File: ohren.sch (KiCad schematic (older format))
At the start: 34 parts, among them J1 Conn_01x18_Male, U1 TLC5951RHA, U2 TLC5951RHA

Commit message: WIP
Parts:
- D10, D11, D12, D14, D15, D17, D4, D5, D6, D7, D8, D9: symbol Device:LED_ARGB -> LED:ASMB-MTB1-0A3A2
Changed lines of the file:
@@
 U1_B1
 $Comp
-L Device:LED_ARGB D6
+L LED:ASMB-MTB1-0A3A2 D6
 U 1 1 5C9EA530
 P 4850 3400
@@
 U1_B2
 $Comp
-L Device:LED_ARGB D7
+L LED:ASMB-MTB1-0A3A2 D7
 U 1 1 5C9EA53F
 P 4850 4250
@@
 	4300 6050 4200 5950
 $Comp
-L Device:LED_ARGB D4
+L LED:ASMB-MTB1-0A3A2 D4
 U 1 1 5CA0D84C
 P 5950 4250
@@
 U1_B4
 $Comp
-L Device:LED_ARGB D5
+L LED:ASMB-MTB1-0A3A2 D5
 U 1 1 5CA0D85B
 P 4850 6150
@@
 	4300 6500 5400 6500
 $Comp
-L Device:LED_ARGB D8
+L LED:ASMB-MTB1-0A3A2 D8
 U 1 1 5CA14C02
 P 5950 5300
@@
 U1_B6
 $Comp
-L Device:LED_ARGB D9
+L LED:ASMB-MTB1-0A3A2 D9
 U 1 1 5CA14C11
 P 5950 6150
@@
 Connection ~ 6300 5300
 $Comp
-L Device:LED_ARGB D10
+L LED:ASMB-MTB1-0A3A2 D10
 U 1 1 5CA31CCE
 P 10450 6150
@@
 U2_B0
 $Comp
-L Device:LED_ARGB D11
+L LED:ASMB-MTB1-0A3A2 D11
 U 1 1 5CA31D33
 P 10450 5300
@@
 U2_B1
 $Comp
-L Device:LED_ARGB D14
+L LED:ASMB-MTB1-0A3A2 D14
 U 1 1 5CA31D42
 P 9350 6150
@@
 U2_B6
 $Comp
-L Device:LED_ARGB D17
+L LED:ASMB-MTB1-0A3A2 D17
 U 1 1 5CA31DD4
 P 9350 3400
@@
 	3700 1200 4000 1200
 $Comp
-L Device:LED_ARGB D15
+L LED:ASMB-MTB1-0A3A2 D15
 U 1 1 5CA31D51
 P 10450 4250
@@
 	8900 4050 9150 4050
 $Comp
-L Device:LED_ARGB D12
+L LED:ASMB-MTB1-0A3A2 D12
 U 1 1 5CA31D9B
 P 10450 3400
@@
 Wire Wire Line
 	4550 1300 4250 1300
+Connection ~ 4550 1000
+Connection ~ 4550 1300
 Wire Bus Line
 	5400 2750 5400 4550
@@
 Wire Bus Line
 	2350 3050 2350 6850
-Connection ~ 4550 1000
-Connection ~ 4550 1300
 $EndSCHEMATC

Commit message: WIP
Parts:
- removed D17: LED_ARGB, LED_SMD:LED_Cree-PLCC4_3.2x2.8mm_CCW, symbol LED:ASMB-MTB1-0A3A2
- removed J1: Conn_01x18_Male, catear-pcb:solder_conn18, symbol Connector:Conn_01x18_Male
- added D1, D2: LED, catear-pcb:smd_led_universal, symbol Device:LED
- added D13, D3: LED_ARGB, LED_SMD:LED_Cree-PLCC4_3.2x2.8mm_CCW, symbol LED:ASMB-MTB1-0A3A2
- added J1: Conn_01x19_MountingPin, catear-pcb:Molex_Easy-On_54550-1971_1x19_P0.5mm_Horizontal, symbol Connector_Generic_MountingPin:Conn_01x19_MountingPin
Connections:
- wire segments 244 -> 247
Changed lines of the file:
@@
 Text Label 10000 5500 0    50   ~ 0
 U2_B6
-$Comp
-L LED:ASMB-MTB1-0A3A2 D17
-U 1 1 5CA31DD4
-P 9350 3400
-F 0 "D17" H 9350 3897 50  0000 C CNN
-F 1 "LED_ARGB" H 9350 3806 50  0000 C CNN
-F 2 "LED_SMD:LED_Cree-PLCC4_3.2x2.8mm_CCW" H 9350 3350 50  0001 C CNN
-F 3 "~" H 9350 3350 50  0001 C CNN
-	1    9350 3400
-	1    0    0    -1
-$EndComp
 Entry Wire Line
 	9900 6050 10000 5950
@@
 	5500 4450 5750 4450
 Wire Wire Line
-	1300 1200 1900 1200
+	1300 1200 1600 1200
 Text Label 3700 1750 1    50   ~ 0
 U1_G4
@@
 Wire Wire Line
 	2500 1500 2500 1750
-$Comp
-L Connector:Conn_01x18_Male J1
-U 1 1 5CDF8D04
-P 550 2200
-F 0 "J1" V 385 2128 50  0000 C CNN
-F 1 "Conn_01x18_Male" V 476 2128 50  0000 C CNN
-F 2 "catear-pcb:solder_conn18" H 550 2200 50  0001 C CNN
-F 3 "~" H 550 2200 50  0001 C CNN
-	1    550  2200
-	0    1    1    0
-$EndComp
 Wire Wire Line
 	-350 2400 -350 2550
@@
 	1800 2550 1800 2250
 Wire Wire Line
-	1800 2550 1350 2550
+	1800 2550 1650 2550
 Wire Wire Line
 	1250 2550 1250 2400
@@
 	1050 2400 1050 2750
 Wire Wire Line
-	2000 2650 950  2650
-Wire Wire Line
 	950  2650 950  2400
 Wire Wire Line
@@
 Connection ~ 4550 1000
 Connection ~ 4550 1300
+$Comp
+L Connector_Generic_MountingPin:Conn_01x19_MountingPin J1
+U 1 1 5CBA6D41
+P 550 2200
+F 0 "J1" V 775 2118 50  0000 C CNN
+F 1 "Conn_01x19_MountingPin" V 684 2118 50  0000 C CNN
+F 2 "catear-pcb:Molex_Easy-On_54550-1971_1x19_P0.5mm_Horizontal" H 550 2200 50  0001 C CNN
+F 3 "~" H 550 2200 50  0001 C CNN
+	1    550  2200
+	0    -1   -1   0
+$EndComp
+$Comp
+L Device:LED D2
+U 1 1 5CBB1488
+P 1600 1350
+F 0 "D2" V 1639 1233 50  0000 R CNN
+F 1 "LED" V 1548 1233 50  0000 R CNN
+F 2 "catear-pcb:smd_led_universal" H 1600 1350 50  0001 C CNN
+F 3 "~" H 1600 1350 50  0001 C CNN
+	1    1600 1350
+	0    -1   -1   0
+$EndComp
+Connection ~ 1600 1200
+Wire Wire Line
+	1600 1200 1900 1200
+$Comp
+L Device:LED D1
+U 1 1 5CBB1D47
+P 1300 1350
+F 0 "D1" V 1339 1233 50  0000 R CNN
+F 1 "LED" V 1248 1233 50  0000 R CNN
+F 2 "catear-pcb:smd_led_universal" H 1300 1350 50  0001 C CNN
+F 3 "~" H 1300 1350 50  0001 C CNN
+	1    1300 1350
+	0    -1   -1   0
+$EndComp
+Connection ~ 1300 1200
+$Comp
+L LED:ASMB-MTB1-0A3A2 D3
+U 1 1 5CBB4B97
+P 5950 3400
+F 0 "D3" H 5950 3897 50  0000 C CNN
+F 1 "LED_ARGB" H 5950 3806 50  0000 C CNN
+F 2 "LED_SMD:LED_Cree-PLCC4_3.2x2.8mm_CCW" H 5950 3350 50  0001 C CNN
+F 3 "~" H 5950 3350 50  0001 C CNN
+	1    5950 3400
+	1    0    0    -1
+$EndComp
+$Comp
+L LED:ASMB-MTB1-0A3A2 D13
+U 1 1 5CBB539C
+P 9350 4250
+F 0 "D13" H 9350 4747 50  0000 C CNN
+F 1 "LED_ARGB" H 9350 4656 50  0000 C CNN
+F 2 "LED_SMD:LED_Cree-PLCC4_3.2x2.8mm_CCW" H 9350 4200 50  0001 C CNN
+F 3 "~" H 9350 4200 50  0001 C CNN
+	1    9350 4250
+	1    0    0    -1
+$EndComp
+Wire Wire Line
+	950  2650 2000 2650
+Wire Wire Line
+	1650 2550 1650 2200
 Wire Bus Line
 	5400 2750 5400 4550
@@
 Wire Bus Line
 	2350 3050 2350 6850
+Connection ~ 1650 2550
+Wire Wire Line
+	1650 2550 1350 2550
 $EndSCHEMATC

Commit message: Almost (tm) finish full rerouting
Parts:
- removed D1, D2: LED, catear-pcb:smd_led_universal, symbol Device:LED
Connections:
- wire segments 247 -> 246
- no-connect marks 1 -> 0
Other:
- moved on the sheet: D10, D11, D12, D13, D14, D15, D3, D4, D5, D6, D8, D9

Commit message: Finish layouting
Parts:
- removed C10, C9: C, Capacitor_SMD:C_1206_3216Metric, symbol Device:C
- removed C6: C, Capacitor_SMD:C_1210_3225Metric, symbol Device:C
- added C6: C, Capacitor_SMD:C_1210_3225Metric, symbol Device:C
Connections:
- wire segments 246 -> 245
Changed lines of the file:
@@
 Wire Wire Line
 	7350 4150 6950 4150
-$Comp
-L Device:C C6
-U 1 1 5C9DBD6E
-P 5150 1150
-F 0 "C6" H 5265 1196 50  0000 L CNN
-F 1 "C" H 5265 1105 50  0000 L CNN
-F 2 "Capacitor_SMD:C_1210_3225Metric" H 5188 1000 50  0001 C CNN
-F 3 "~" H 5150 1150 50  0001 C CNN
-	1    5150 1150
-	1    0    0    -1
-$EndComp
 Wire Wire Line
 	5150 900  5150 1000
@@
 Text Label 1800 3150 0    50   ~ 0
 DCSOUT
-Text Label 1800 3450 0    50   ~ 0
+Text Label 1800 3750 0    50   ~ 0
 GSSIN
-Text Label 1800 3350 0    50   ~ 0
+Text Label 1800 3650 0    50   ~ 0
 DCSIN
 Text Label 1800 3550 0    50   ~ 0
 GSSCK
-Text Label 1450 4400 0    50   ~ 0
+Text Label 1800 3450 0    50   ~ 0
 DCSCK
-Text Label 1800 4500 0    50   ~ 0
+Text Label 1800 3350 0    50   ~ 0
 XBLNK
-Text Label 1800 3750 0    50   ~ 0
+Text Label 1800 3950 0    50   ~ 0
 GSCKR
-Text Label 1800 3850 0    50   ~ 0
+Text Label 1800 4050 0    50   ~ 0
 GSCKG
-Text Label 1800 3950 0    50   ~ 0
+Text Label 1800 4150 0    50   ~ 0
 GSCKB
 Entry Wire Line
@@
 Entry Wire Line
 	2350 4350 2450 4250
-$Comp
-L Device:C C9
-U 1 1 5D009474
-P 4550 1150
-F 0 "C9" H 4668 1196 50  0000 L CNN
-F 1 "C" H 4668 1105 50  0000 L CNN
-F 2 "Capacitor_SMD:C_1206_3216Metric" H 4588 1000 50  0001 C CNN
-F 3 "~" H 4550 1150 50  0001 C CNN
-	1    4550 1150
-	1    0    0    -1
-$EndComp
-$Comp
-L Device:C C10
-U 1 1 5D01A6A4
-P 6050 1150
-F 0 "C10" H 6168 1196 50  0000 L CNN
-F 1 "C" H 6168 1105 50  0000 L CNN
-F 2 "Capacitor_SMD:C_1206_3216Metric" H 6088 1000 50  0001 C CNN
-F 3 "~" H 6050 1150 50  0001 C CNN
-	1    6050 1150
-	1    0    0    -1
-$EndComp
-Wire Wire Line
-	6050 1000 5750 1000
-Connection ~ 5750 1000
-Wire Wire Line
-	6050 1300 5750 1300
-Connection ~ 5750 1300
-Wire Wire Line
-	4850 1000 4550 1000
 Connection ~ 4850 1000
-Wire Wire Line
-	4850 1300 4550 1300
 Connection ~ 4850 1300
 $Comp
@@
 	1800 2550 1800 2250
 Wire Wire Line
-	1800 2550 1650 2550
-Wire Wire Line
 	1350 2400 1350 2550
 Wire Wire Line
@@
 	1900 2850 1900 2750
 Wire Wire Line
-	1900 2750 1250 2750
+	1900 2750 1700 2750
 Connection ~ 1250 2750
 Wire Wire Line
@@
 Wire Wire Line
 	2000 2250 2000 2650
-Text Label 1800 3650 0    50   ~ 0
+Text Label 1800 3850 0    50   ~ 0
 GSLAT
 Wire Wire Line
-	2250 3350 650  3350
-Wire Wire Line
-	650  3350 650  2400
-Wire Wire Line
-	2250 3450 550  3450
-Wire Wire Line
-	550  3450 550  2400
-Wire Wire Line
-	2250 3550 450  3550
-Wire Wire Line
-	450  3550 450  2400
-Wire Wire Line
-	2250 3650 350  3650
-Wire Wire Line
-	350  3650 350  2400
-Wire Wire Line
-	2250 3750 250  3750
-Wire Wire Line
-	250  3750 250  2400
-Wire Wire Line
 	2250 3850 250  3850
 Wire Wire Line
-	250  3850 250  3750
-Connection ~ 250  3750
-Wire Wire Line
-	2250 3950 250  3950
-Wire Wire Line
-	250  3950 250  3850
-Connection ~ 250  3850
-Wire Wire Line
-	2250 4050 150  4050
-Wire Wire Line
-	150  4050 150  2400
-Wire Wire Line
 	2250 4150 50   4150
-Wire Wire Line
-	50   4150 50   2400
 Text Label 1900 1750 1    50   ~ 0
 U2_R4
@@
 	1    0    0    -1
 $EndComp
-Wire Wire Line
-	4550 1000 4250 1000
-Wire Wire Line
-	4550 1300 4250 1300
-Connection ~ 4550 1000
-Connection ~ 4550 1300
 $Comp
 L Connector_Generic_MountingPin:Conn_01x19_MountingPin J1
@@
 $EndComp
 Wire Wire Line
-	1650 2550 1650 2200
-Connection ~ 1650 2550
-Wire Wire Line
-	1650 2550 1450 2550
-Wire Wire Line
 	1300 1200 1900 1200
 Wire Wire Line
@@
 Wire Wire Line
 	950  3250 950  2400
+Wire Wire Line
+	50   4150 50   4050
+Connection ~ 50   4050
+Wire Wire Line
+	50   4050 50   3950
+Wire Wire Line
+	50   3950 2250 3950
+Connection ~ 50   3950
+Wire Wire Line
+	50   3950 50   2400
+Wire Wire Line
+	-50  2650 150  2650
+Wire Wire Line
+	150  2650 150  2400
+Connection ~ -50  2650
+Wire Wire Line
+	50   4050 2250 4050
+Wire Wire Line
+	250  3850 250  2400
+Wire Wire Line
+	2250 3750 350  3750
+Wire Wire Line
+	350  3750 350  2400
+Wire Wire Line
+	2250 3650 450  3650
+Wire Wire Line
+	450  3650 450  2400
+Wire Wire Line
+	2250 3550 550  3550
+Wire Wire Line
+	550  3550 550  2400
+Wire Wire Line
+	2250 3450 650  3450
+Wire Wire Line
+	650  3450 650  2400
+Wire Wire Line
+	2250 3350 750  3350
+Wire Wire Line
+	750  3350 750  2400
+Wire Wire Line
+	1450 2550 1800 2550
+Wire Wire Line
+	1650 2200 1700 2200
+Wire Wire Line
+	1700 2200 1700 2750
+Connection ~ 1700 2750
+Wire Wire Line
+	1700 2750 1250 2750
+Wire Wire Line
+	4250 1000 4850 1000
+Wire Wire Line
+	4250 1300 4850 1300
+$Comp
+L Device:C C6
+U 0 0 5D11A988
+P 5150 1150
+F 0 "C6" H 5265 1196 50  0000 L CNN
+F 1 "C" H 5265 1105 50  0000 L CNN
+F 2 "Capacitor_SMD:C_1210_3225Metric" H 5188 1000 50  0001 C CNN
+F 3 "~" H 5150 1150 50  0001 C CNN
+	0    5150 1150
+	1    0    0    -1
+$EndComp
 Wire Bus Line
 	5400 2750 5400 4550

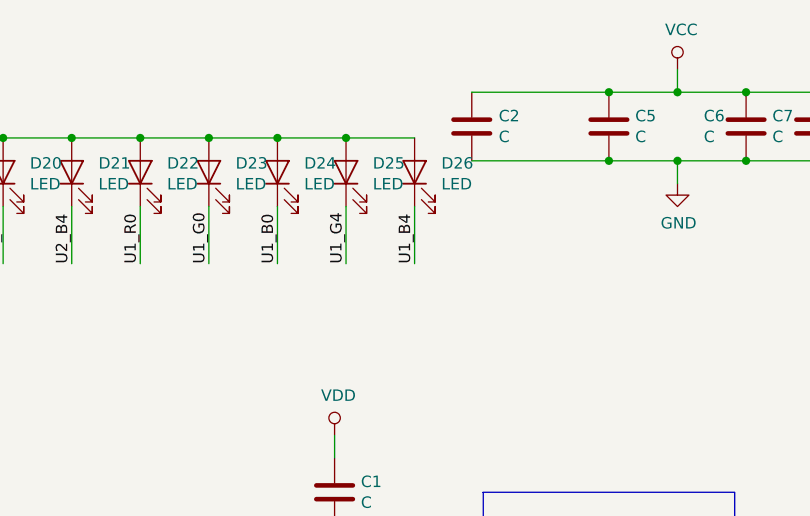
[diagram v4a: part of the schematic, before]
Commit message: Adjust UV LED attachment + U1 LED routing slightly
Slight changes for better groundplane coverage
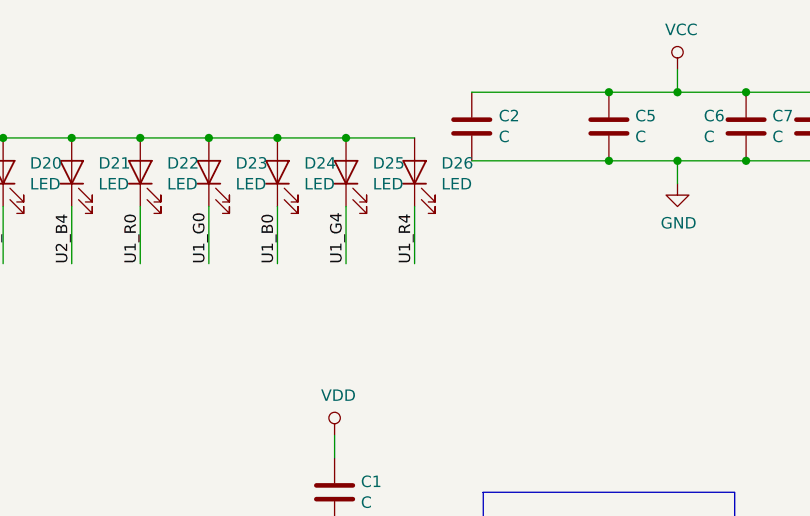
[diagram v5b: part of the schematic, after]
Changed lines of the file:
@@
 	3700 1500 3700 1750
 Text Label 4000 1750 1    50   ~ 0
-U1_B4
+U1_R4
 Wire Wire Line
 	4000 1500 4000 1750
